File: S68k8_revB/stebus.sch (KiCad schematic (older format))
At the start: 24 parts, among them J1 Connector_DIN41612_2x32, U1 ATF16V8C, U2 74LS245, U3 74LS541, U4 74LS244, U5 74LS541, U6 74LS541, U7 74LS07, U8 74LS245

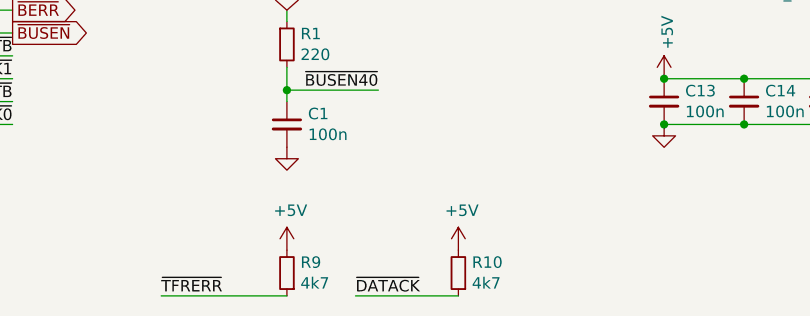
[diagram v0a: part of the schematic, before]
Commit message: S68k8: change pull-up for DTACK to a separate resistor
Tests show 4k7 is too large to pull the line back fast enough. Reducing to 1k or even 470R give much better results.
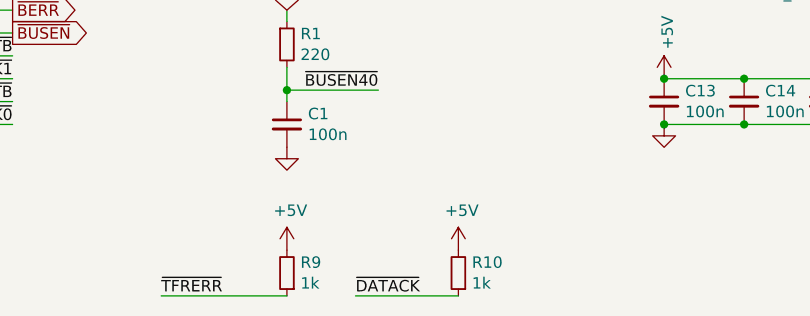
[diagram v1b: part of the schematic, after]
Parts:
- R10, R9: value 4k7 -> 1k
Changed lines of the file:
@@
 P 5350 7000
 F 0 "R9" H 5291 6954 50  0000 R CNN
-F 1 "4k7" H 5291 7045 50  0000 R CNN
+F 1 "1k" H 5291 7045 50  0000 R CNN
 F 2 "Resistor_THT:R_Axial_DIN0204_L3.6mm_D1.6mm_P7.62mm_Horizontal" H 5350 7000 50  0001 C CNN
 F 3 "~" H 5350 7000 50  0001 C CNN
@@
 P 6100 7000
 F 0 "R10" H 6041 6954 50  0000 R CNN
-F 1 "4k7" H 6041 7045 50  0000 R CNN
+F 1 "1k" H 6041 7045 50  0000 R CNN
 F 2 "Resistor_THT:R_Axial_DIN0204_L3.6mm_D1.6mm_P7.62mm_Horizontal" H 6100 7000 50  0001 C CNN
 F 3 "~" H 6100 7000 50  0001 C CNN

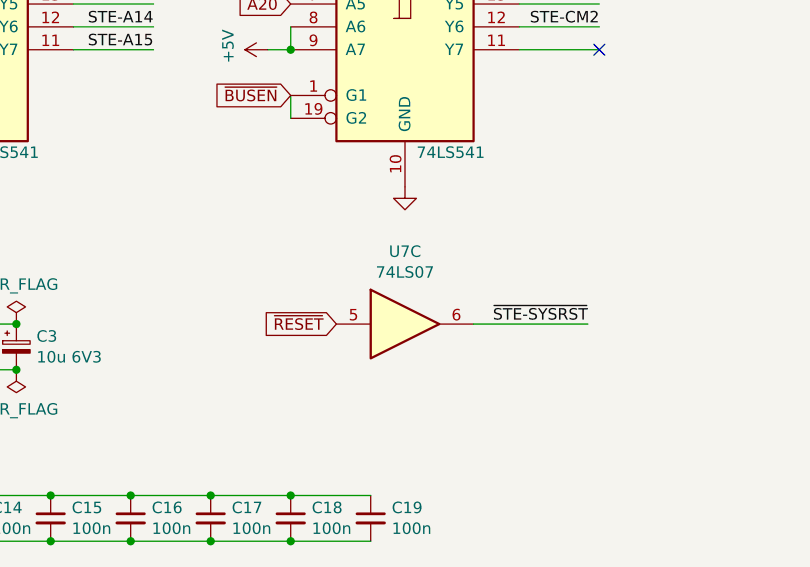
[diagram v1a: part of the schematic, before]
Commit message: S68k8: moved copper pours for power distribution to the bottom layer
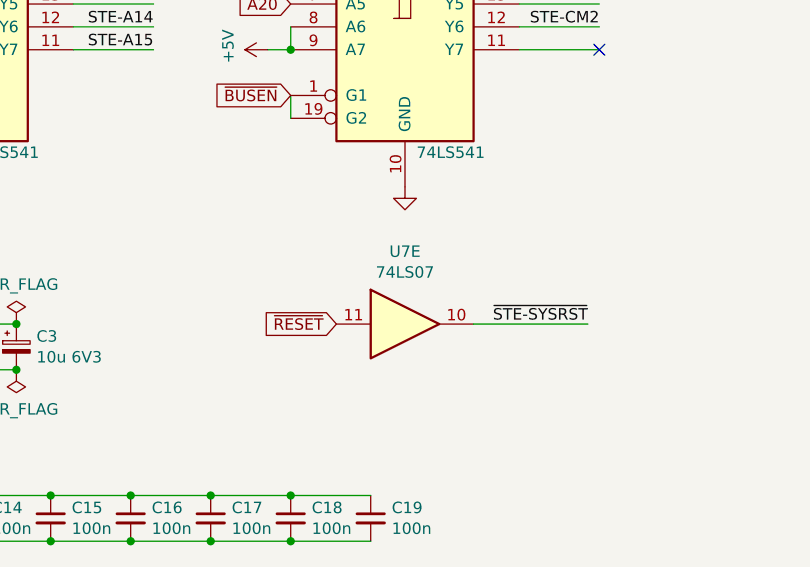
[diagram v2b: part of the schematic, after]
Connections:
- net ~RESET: now also U7.11; no longer U7.5
- net ~STE-SYSRST: now also U7.10; no longer U7.6
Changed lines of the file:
@@
 $Comp
 L 74xx:74LS07 U7
-U 3 1 60759A4C
+U 5 1 60759A4C
 P 9250 5400
 F 0 "U7" H 9250 5717 50  0000 C CNN
@@
 F 2 "Package_DIP:DIP-14_W7.62mm" H 9250 5400 50  0001 C CNN
 F 3 "www.ti.com/lit/ds/symlink/sn74ls07.pdf" H 9250 5400 50  0001 C CNN
-	3    9250 5400
+	5    9250 5400
 	1    0    0    -1
 $EndComp
